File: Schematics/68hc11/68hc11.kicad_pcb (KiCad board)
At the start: 2 copper layers, 268.6 x 177.2 mm, 37 parts, among them J1 DC 5 Volts, J2 DB9_Female, J3 Screw_Terminal_01x10, J4 Screw_Terminal_01x10, J5 Screw_Terminal_01x10, J6 Screw_Terminal_01x10, SW1 Reset, U1 MC68HC11A1CC-PLLC, U10 MCP100-270D, U2 MC68B21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

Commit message: Playing with free routing tool
ripped it all out when finished
Still need to add address decode hardware then try again.
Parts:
- moved U2 86.4 mm to (193.5, 134.7)
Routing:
- net /A11: track 59.2 -> 0.00 mm
- net /A9: track 59.0 -> 0.00 mm
- net /A10: track 56.5 -> 0.00 mm
- net /A8: track 56.1 -> 0.00 mm
- net /A12: track 56.0 -> 0.00 mm
- net /D2: track 52.3 -> 0.00 mm
- net /A3: track 52.3 -> 0.00 mm
- net /A2: track 52.2 -> 0.00 mm
- net /A5: track 52.2 -> 0.00 mm
- net /A6: track 52.2 -> 0.00 mm
- net /D6: track 52.1 -> 0.00 mm
- net /A7: track 52.0 -> 0.00 mm
- net /D5: track 52.0 -> 0.00 mm
- net /D7: track 52.0 -> 0.00 mm
- net /D4: track 52.0 -> 0.00 mm
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- removed copper zone on B.Cu, net GND
- removed copper zone on F.Cu, net VCC

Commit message: Added address logic chips
Next is layout
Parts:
- added C10: 0.1uF, Capacitor_THT:C_Disc_D3.0mm_W2.0mm_P2.50mm, F.Cu at (215.5, 31.3)
- added C17: 0.1uF, Capacitor_THT:C_Disc_D3.0mm_W2.0mm_P2.50mm, F.Cu at (227.2, 30.7)
- added C18: 0.1uF, Capacitor_THT:C_Disc_D3.0mm_W2.0mm_P2.50mm, F.Cu at (262.5, 31.4)
- added C19: 0.1uF, Capacitor_THT:C_Disc_D3.0mm_W2.0mm_P2.50mm, F.Cu at (275.6, 30.9)
- added C20: 0.1uF, Capacitor_THT:C_Disc_D3.0mm_W2.0mm_P2.50mm, F.Cu at (251.0, 31.4)
- added C21: 0.1uF, Capacitor_THT:C_Disc_D3.0mm_W2.0mm_P2.50mm, F.Cu at (239.2, 31.4)
- added U11: 74LS138, Package_DIP:DIP-16_W7.62mm_Socket, F.Cu at (219.7, 35.0)
- added U12: 74LS21, Package_DIP:DIP-14_W7.62mm_Socket, F.Cu at (231.4, 35.0)
- added U13: 74LS32, Package_DIP:DIP-14_W7.62mm_Socket, F.Cu at (254.9, 35.0)
- added U14: 74LS32, Package_DIP:DIP-14_W7.62mm_Socket, F.Cu at (267.9, 35.0)
- added U15: 74LS04, Package_DIP:DIP-14_W7.62mm_Socket, F.Cu at (243.2, 35.0)
- added U5: 74LS138, Package_DIP:DIP-16_W7.62mm_Socket, F.Cu at (207.9, 35.0)
- J1: footprint Connector_BarrelJack:BarrelJack_CUI_PJ-063AH_Horizontal_CircularHoles -> digikey-footprints:Barrel_Jack_5.5mmODx2.1mmID_PJ-102A
- moved C8 149.6 mm to (108.2, 102.7)
- moved C4 99.3 mm to (149.6, 149.2)
- moved C3 98.6 mm to (137.3, 80.0)
- moved C5 80.3 mm to (182.7, 93.3)
- moved C2 47.3 mm to (194.3, 130.7)
- moved C7 34.4 mm to (82.8, 102.5)

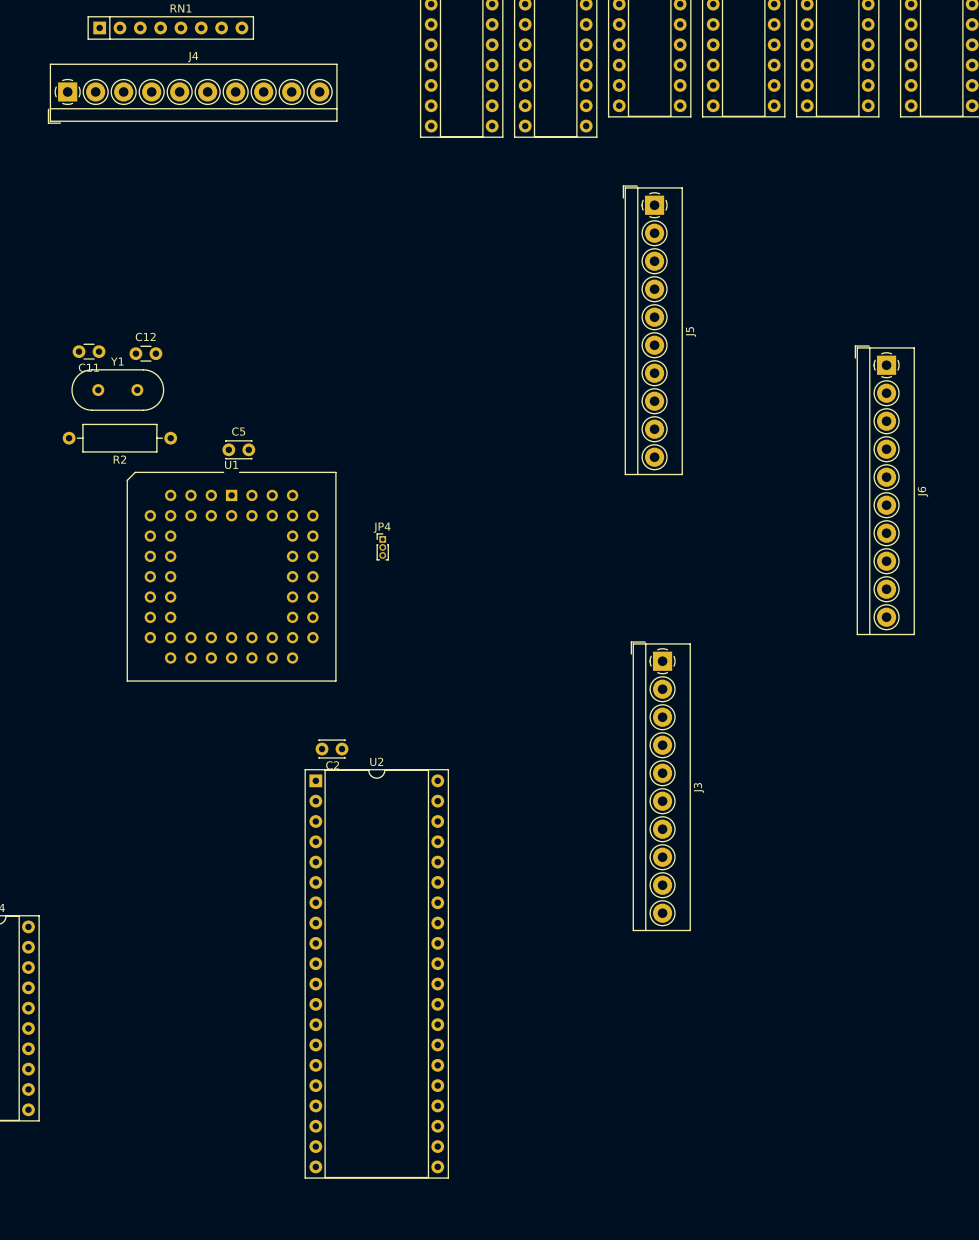
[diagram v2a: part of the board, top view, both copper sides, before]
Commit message: Replaced screw terminals with pin headers
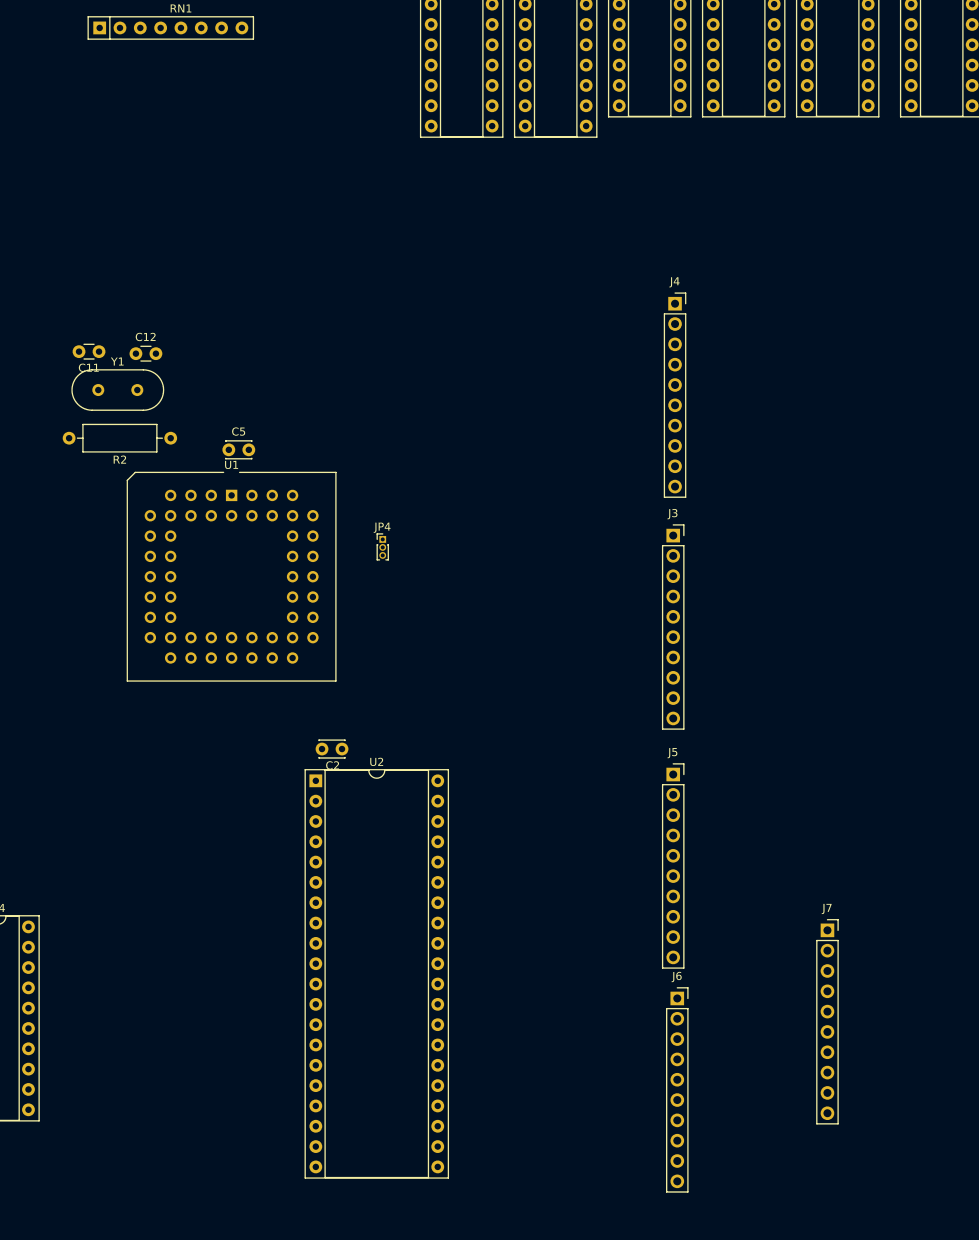
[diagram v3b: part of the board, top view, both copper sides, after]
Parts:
- added J7: Conn_01x10_Male, Connector_PinSocket_2.54mm:PinSocket_1x10_P2.54mm_Vertical, F.Cu at (257.5, 153.4)
- J3, J4, J5, J6: value Screw_Terminal_01x10 -> Conn_01x10_Male; footprint TerminalBlock_4Ucon:TerminalBlock_4Ucon_1x10_P3.50mm_Horizontal -> Connector_PinSocket_2.54mm:PinSocket_1x10_P2.54mm_Vertical
- moved J6 83.4 mm to (238.7, 161.9), turned to 0 degrees
- moved J4 80.4 mm to (238.4, 75.0)
- moved J5 71.2 mm to (238.2, 133.9), turned to 0 degrees
- moved J3 15.8 mm to (238.2, 104.0), turned to 0 degrees
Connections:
- J5 pad 1: /PPA0 -> /CA1
- J5 pad 10: /CA2 -> /PPA7
- J5 pad 2: /PPA1 -> /CA2
- J5 pad 3: /PPA2 -> /PPA0
- J5 pad 4: /PPA3 -> /PPA1
- J5 pad 5: /PPA4 -> /PPA2
- J5 pad 6: /PPA5 -> /PPA3
- J5 pad 7: /PPA6 -> /PPA4
- J5 pad 8: /PPA7 -> /PPA5
- J5 pad 9: /CA1 -> /PPA6
- U8 pad 20: /*RAM -> unconnected-(U8-Pad20)

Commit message: Anouther autorouting attempt
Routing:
- net GND: track 0.00 -> 775.1 mm, vias 0 -> 1
- net VCC: track 0.00 -> 765.4 mm, vias 0 -> 1
- net /R/*W: track 0.00 -> 364.2 mm
- net /*RESET: track 0.00 -> 330.0 mm, vias 0 -> 1
- net /A12: track 0.00 -> 240.6 mm, vias 0 -> 1
- net /*BOOT: track 0.00 -> 227.3 mm
- net /D0: track 0.00 -> 220.9 mm
- net /D1: track 0.00 -> 220.7 mm
- net /A10: track 0.00 -> 218.5 mm
- net /D7: track 0.00 -> 217.6 mm
- net /D2: track 0.00 -> 212.6 mm, vias 0 -> 1
- net /D6: track 0.00 -> 212.2 mm
- net /A11: track 0.00 -> 209.4 mm
- net /D3: track 0.00 -> 208.1 mm, vias 0 -> 1
- net /*SPARE: track 0.00 -> 207.8 mm
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
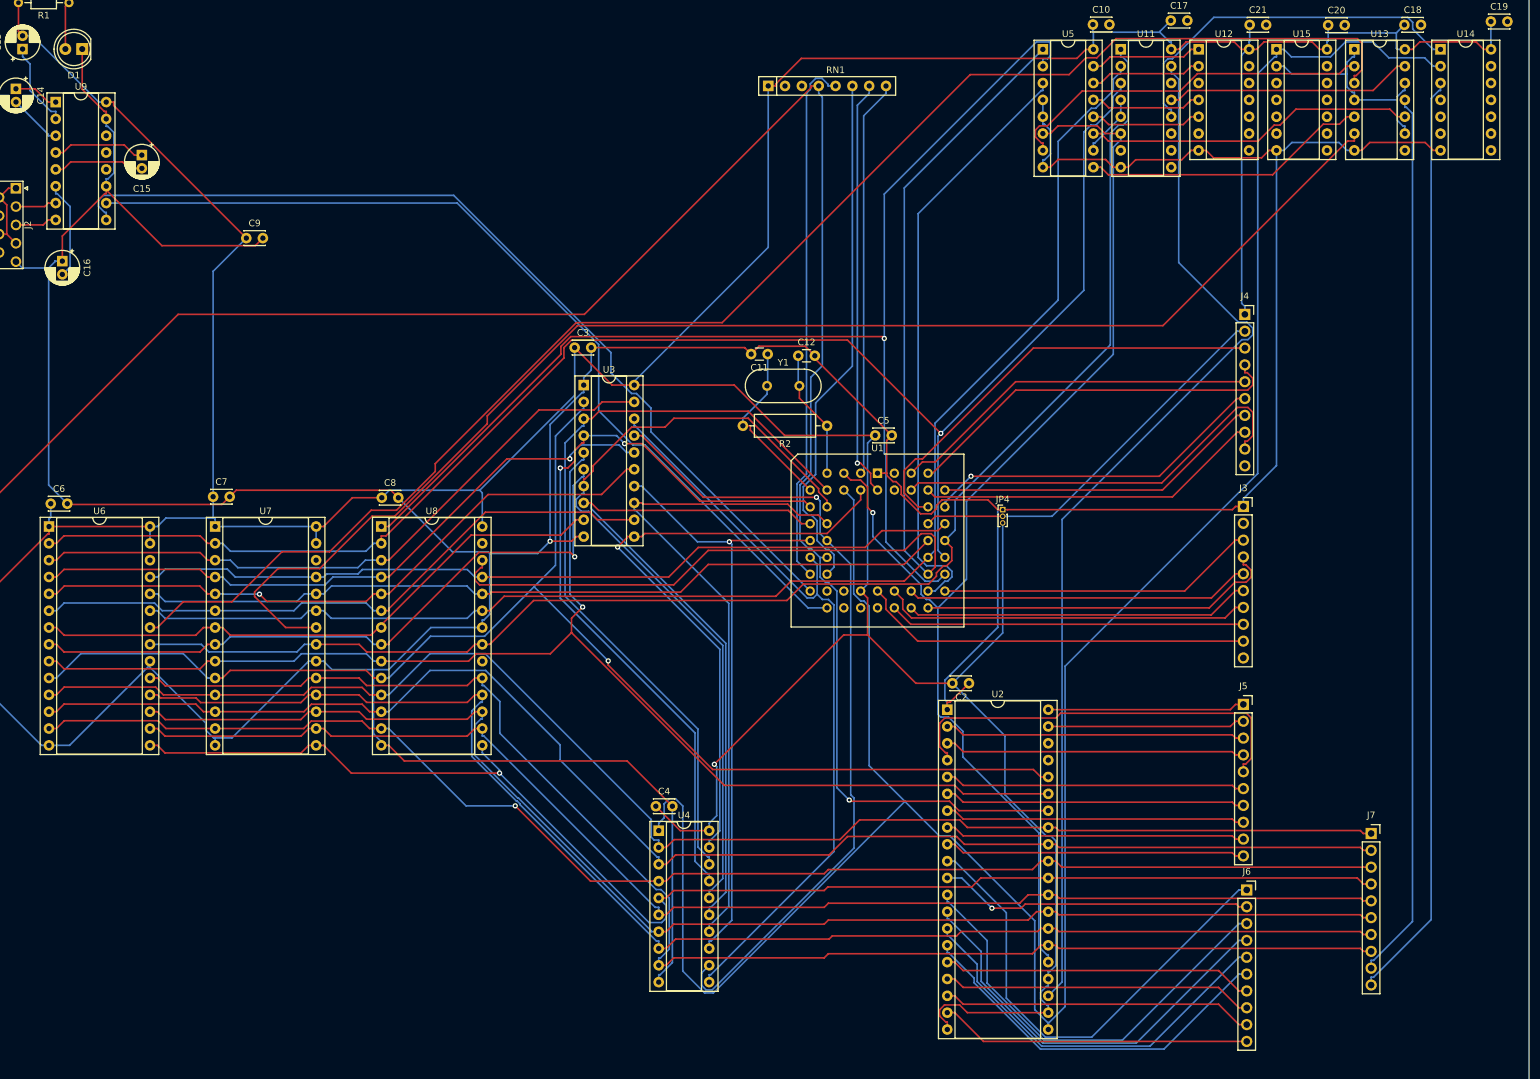
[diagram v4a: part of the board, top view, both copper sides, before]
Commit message: Updated chip footprints and generated new vBOM
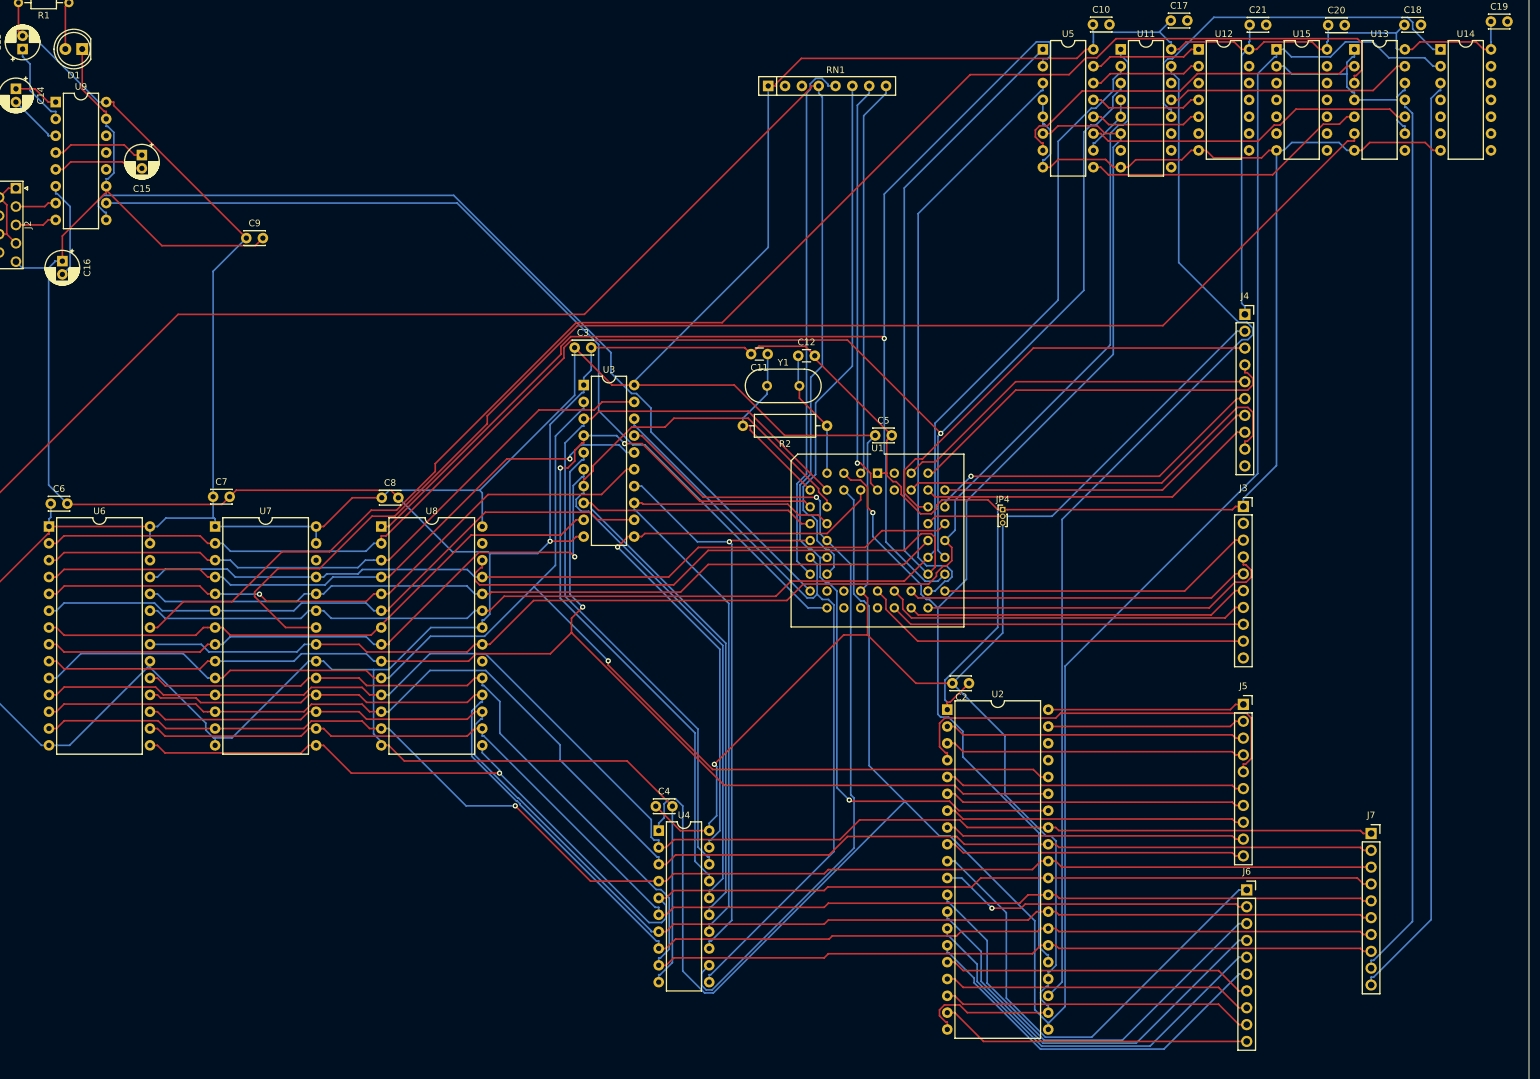
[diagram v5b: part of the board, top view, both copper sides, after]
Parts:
- U11, U5, U9: footprint Package_DIP:DIP-16_W7.62mm_Socket -> Package_DIP:DIP-16_W7.62mm
- U12, U13, U14, U15: footprint Package_DIP:DIP-14_W7.62mm_Socket -> Package_DIP:DIP-14_W7.62mm
- U2: footprint Package_DIP:DIP-40_W15.24mm_Socket -> Package_DIP:DIP-40_W15.24mm
- U3, U4: footprint Package_DIP:DIP-20_W7.62mm_Socket -> Package_DIP:DIP-20_W7.62mm
- U6, U7, U8: footprint Package_DIP:DIP-28_W15.24mm_Socket -> Package_DIP:DIP-28_W15.24mm

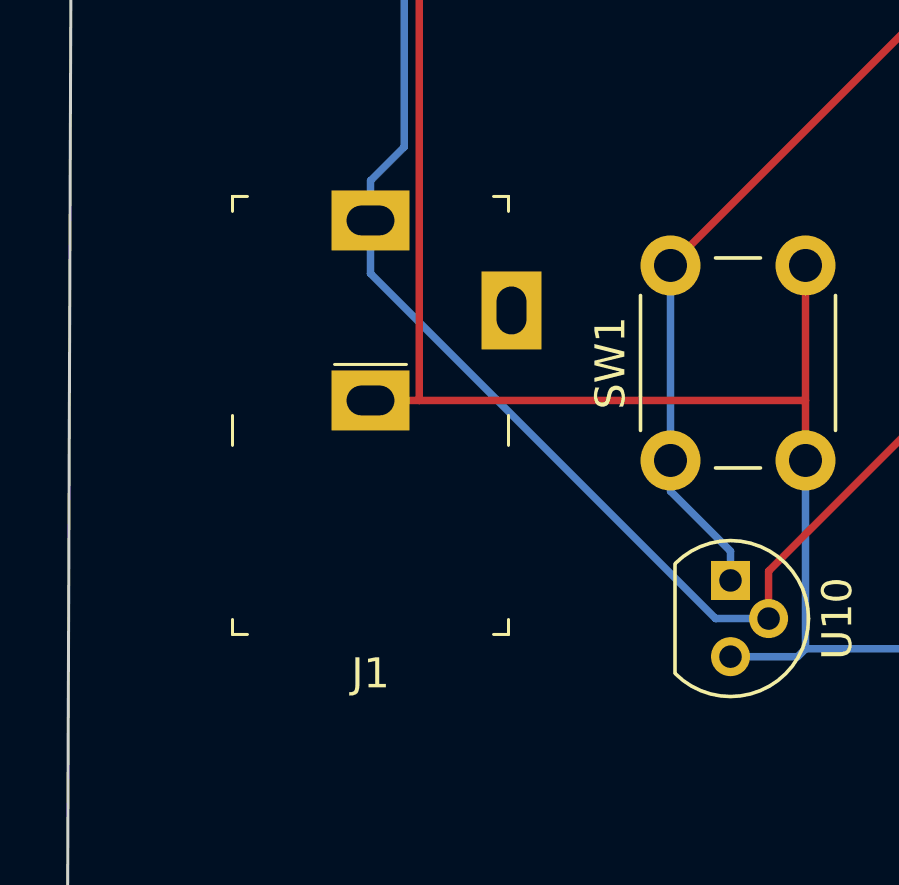
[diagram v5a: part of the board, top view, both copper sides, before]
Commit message: Updated power to micro usb b receptical
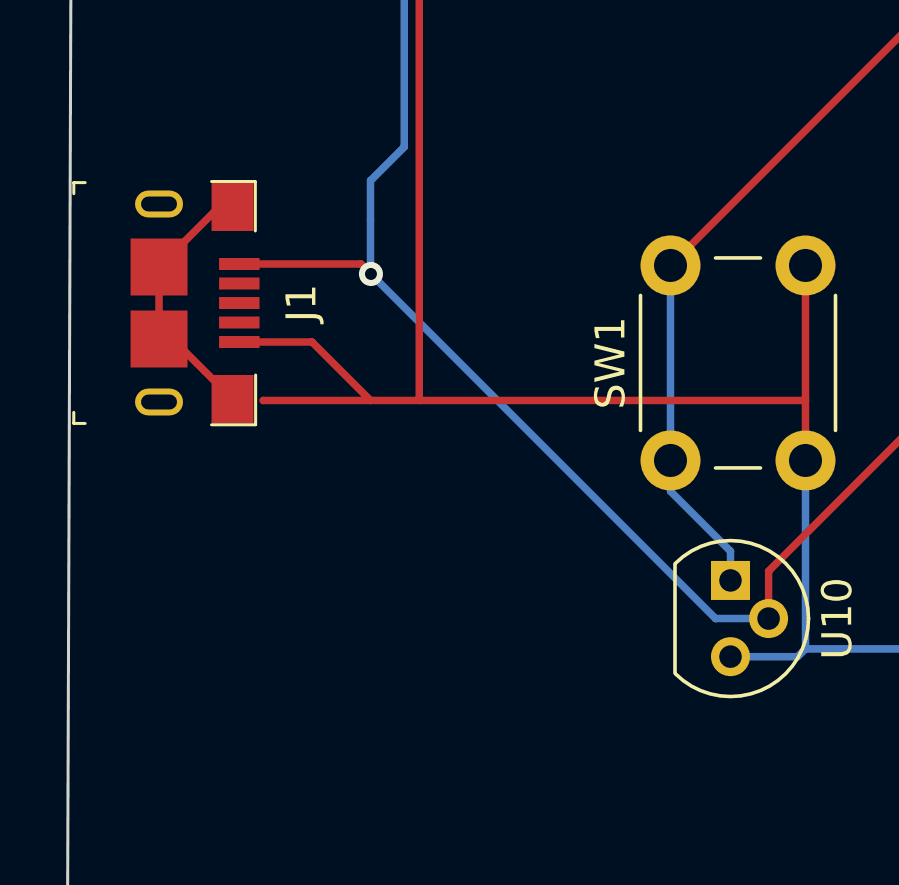
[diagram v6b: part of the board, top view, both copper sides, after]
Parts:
- J1: footprint digikey-footprints:Barrel_Jack_5.5mmODx2.1mmID_PJ-102A -> digikey-footprints:USB_Micro_B_Female_10118193-0001LF
- moved J1 7.05 mm to (16.0, 120.8), turned to -90 degrees
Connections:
- J1 pad 2: GND -> unconnected-(J1-Pad2)
- J1 pad 3: (no net) -> unconnected-(J1-Pad3)
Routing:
- net (no net): track 0.00 -> 8.96 mm
- net GND: track 775.1 -> 783.8 mm
- net VCC: track 765.4 -> 770.0 mm, vias 1 -> 2

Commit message: yET ANOTHER LAYOUT AND ROUTING
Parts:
- J1: value DC 5 Volts -> USB3076-30-A
- J2: footprint Connector_Dsub:DSUB-9_Male_Horizontal_P2.77x2.54mm_EdgePinOffset9.40mm -> Connector_Dsub:DSUB-9_Male_Horizontal_P2.77x2.84mm_EdgePinOffset4.94mm_Housed_MountingHolesOffset7.48mm
- moved J5 123.8 mm to (121.3, 174.5), turned to 90 degrees
- moved J7 108.3 mm to (151.4, 174.9), turned to 90 degrees
- moved U13 89.2 mm to (203.2, 107.7)
- moved C18 88.9 mm to (210.7, 103.6)
- moved C19 85.5 mm to (232.7, 104.8)
- moved U14 85.5 mm to (225.1, 109.0)
- moved C17 81.7 mm to (191.7, 104.2)
- moved U11 80.7 mm to (184.6, 107.8)
- moved J6 58.1 mm to (182.0, 174.7), turned to 90 degrees
- moved U12 56.4 mm to (202.8, 83.6)
- moved C21 55.0 mm to (211.3, 78.8)
- moved C10 52.6 mm to (191.8, 78.2)
- moved U5 52.6 mm to (184.2, 81.9)
- moved U15 51.8 mm to (224.7, 83.5)
- moved C20 51.8 mm to (232.5, 79.8)
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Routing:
- net /R/*W: track 364.2 -> 196.2 mm, vias 0 -> 3
- net VCC: track 770.0 -> 645.4 mm, vias 2 -> 1
- net /*PIA1: track 159.6 -> 42.7 mm
- net /*RESET: track 330.0 -> 216.8 mm, vias 1 -> 3
- net /E: track 184.4 -> 90.7 mm, vias 1 -> 0
- net /*SPARE: track 207.8 -> 115.4 mm, vias 0 -> 1
- net /*BOOT: track 227.3 -> 136.2 mm, vias 0 -> 2
- net /A12: track 240.6 -> 153.7 mm, vias 1 -> 3
- net /A11: track 209.4 -> 124.3 mm, vias 0 -> 1
- net /A10: track 218.5 -> 144.9 mm, vias 0 -> 1
- net /PE6: track 52.3 -> 123.7 mm
- net /A13: track 172.1 -> 103.2 mm, vias 0 -> 1
- net /PA6: track 59.2 -> 123.6 mm, vias 0 -> 2
- net /PA5: track 53.7 -> 116.4 mm, vias 0 -> 1
- net /PA4: track 55.9 -> 112.2 mm, vias 0 -> 1
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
